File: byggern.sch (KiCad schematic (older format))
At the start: 41 parts, among them J1 Power_Rail, J2 JTAG LINK, J3 OLED_Connection, J4 CAN, J5 P1000 Header, J6 DB9_Female_MountingHoles, U1 Barrel_jack, U10 MAX233, U2 LM340SX, U3 ATmega162-16PU, U4 GAL16V8, U5 MCP2515, U6 SN74ALS573CN, U7 MCP2551, U8 IDT7164, U9 ADC0844, Y1 4.9MHz, Y2 16MHz

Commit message: Add footprints to components
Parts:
- D1: footprint (none) -> LED_SMD:LED_0805_2012Metric_Pad1.15x1.40mm_HandSolder
- J6: footprint (none) -> Connector_Dsub:DSUB-9_Female_Vertical_P2.77x2.84mm_MountingHoles
- U10: footprint (none) -> byggern:MAX233CPP
- U2: footprint (none) -> byggern:LM340SX
- U4: footprint (none) -> byggern:GAL16V8
- U5: footprint (none) -> byggern:MCP2515-EP
- U6: footprint (none) -> byggern:SN74ALS573CN
- U7: footprint (none) -> byggern:MCP2551-IP
- U8: footprint (none) -> byggern:CY7C185-20PC
- U9: footprint (none) -> byggern:ADC0844CCN
- Y1, Y2: footprint (none) -> Connector_PinHeader_2.54mm:PinHeader_1x02_P2.54mm_Vertical
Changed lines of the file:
@@
 F 0 "U2" H 1900 6975 50  0000 C CNN
 F 1 "LM340SX" H 1900 6884 50  0000 C CNN
-F 2 "" H 1800 6900 50  0001 C CNN
+F 2 "byggern:LM340SX" H 1800 6900 50  0001 C CNN
 F 3 "" H 1800 6900 50  0001 C CNN
 	1    1800 6900
@@
 F 0 "D1" V 2889 7132 50  0000 R CNN
 F 1 "PWR_LED" V 2798 7132 50  0000 R CNN
-F 2 "" H 2850 7250 50  0001 C CNN
+F 2 "LED_SMD:LED_0805_2012Metric_Pad1.15x1.40mm_HandSolder" H 2850 7250 50  0001 C CNN
 F 3 "~" H 2850 7250 50  0001 C CNN
 	1    2850 7250
@@
 F 0 "Y1" V 954 2381 50  0000 L CNN
 F 1 "4.9MHz" V 1045 2381 50  0000 L CNN
-F 2 "" H 1000 2250 50  0001 C CNN
+F 2 "Connector_PinHeader_2.54mm:PinHeader_1x02_P2.54mm_Vertical" H 1000 2250 50  0001 C CNN
 F 3 "~" H 1000 2250 50  0001 C CNN
 	1    1000 2250
@@
 F 0 "U10" H 10000 3450 50  0000 C CNN
 F 1 "MAX233" H 10100 3350 50  0000 C CNN
-F 2 "" H 9300 3450 50  0001 C CNN
+F 2 "byggern:MAX233CPP" H 9300 3450 50  0001 C CNN
 F 3 "" H 9300 3450 50  0001 C CNN
 	1    9550 3650
@@
 F 0 "J6" H 10700 6100 50  0000 L CNN
 F 1 "DB9_Female_MountingHoles" H 10700 6000 50  0000 L CNN
-F 2 "" H 11000 5400 50  0001 C CNN
+F 2 "Connector_Dsub:DSUB-9_Female_Vertical_P2.77x2.84mm_MountingHoles" H 11000 5400 50  0001 C CNN
 F 3 " ~" H 11000 5400 50  0001 C CNN
 	1    11000 5400
@@
 F 0 "U4" H 4450 4950 50  0000 C CNN
 F 1 "GAL16V8" H 4550 4850 50  0000 C CNN
-F 2 "" H 4350 4250 50  0001 C CNN
+F 2 "byggern:GAL16V8" H 4350 4250 50  0001 C CNN
 F 3 "" H 4350 4250 50  0001 C CNN
 	1    4350 4250
@@
 F 0 "U8" H 7050 2850 50  0000 L CNN
 F 1 "IDT7164" H 7050 2750 50  0000 L CNN
-F 2 "" H 6700 3150 50  0001 C CNN
+F 2 "byggern:CY7C185-20PC" H 6700 3150 50  0001 C CNN
 F 3 "" H 6700 3150 50  0001 C CNN
 	1    6700 2050
@@
 F 0 "U6" H 5700 1650 50  0000 C CNN
 F 1 "SN74ALS573CN" H 5900 1550 50  0000 C CNN
-F 2 "" H 5450 1450 50  0001 C CNN
+F 2 "byggern:SN74ALS573CN" H 5450 1450 50  0001 C CNN
 F 3 "" H 5450 1450 50  0001 C CNN
 	1    5450 1400
@@
 F 0 "U9" H 8750 1450 50  0000 C CNN
 F 1 "ADC0844" H 8850 1350 50  0000 C CNN
-F 2 "" H 8800 1350 50  0001 C CNN
+F 2 "byggern:ADC0844CCN" H 8800 1350 50  0001 C CNN
 F 3 "" H 8800 1350 50  0001 C CNN
 	1    8450 1350
@@
 F 0 "U5" H 4900 5650 50  0000 C CNN
 F 1 "MCP2515" H 5050 5550 50  0000 C CNN
-F 2 "" H 4700 5750 50  0001 C CNN
+F 2 "byggern:MCP2515-EP" H 4700 5750 50  0001 C CNN
 F 3 "" H 4700 5750 50  0001 C CNN
 	1    4700 5750
@@
 F 0 "Y2" V 3950 7250 50  0000 R CNN
 F 1 "16MHz" V 3850 7250 50  0000 R CNN
-F 2 "" H 3850 6900 50  0001 C CNN
+F 2 "Connector_PinHeader_2.54mm:PinHeader_1x02_P2.54mm_Vertical" H 3850 6900 50  0001 C CNN
 F 3 "~" H 3850 6900 50  0001 C CNN
 	1    3850 6900
@@
 F 0 "U7" H 6600 5150 50  0000 C CNN
 F 1 "MCP2551" H 6700 5050 50  0000 C CNN
-F 2 "" H 6350 5500 50  0001 C CNN
+F 2 "byggern:MCP2551-IP" H 6350 5500 50  0001 C CNN
 F 3 "" H 6350 5500 50  0001 C CNN
 	1    6350 5500

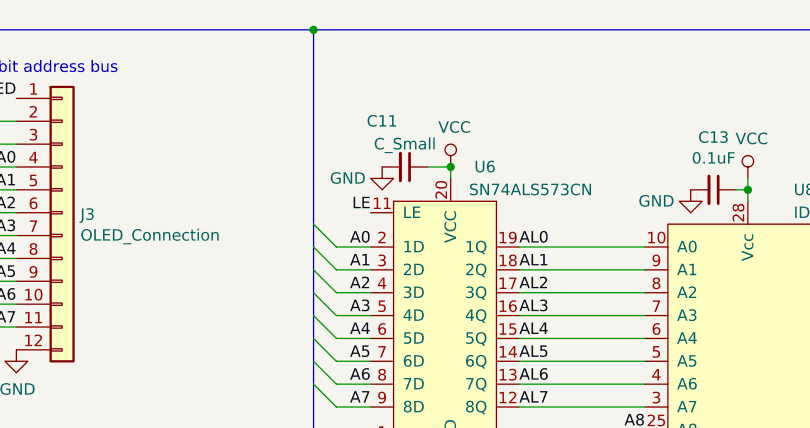
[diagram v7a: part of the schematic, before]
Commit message: Start routing PCB
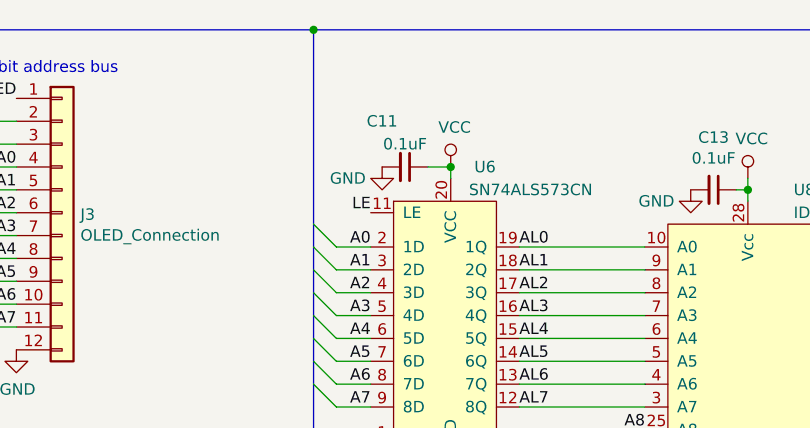
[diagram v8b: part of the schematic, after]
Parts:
- C11: value C_Small -> 0.1uF
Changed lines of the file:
@@
 P 5350 1150
 F 0 "C11" V 5150 1050 50  0000 C CNN
-F 1 "C_Small" V 5250 1150 50  0000 C CNN
+F 1 "0.1uF" V 5250 1150 50  0000 C CNN
 F 2 "Capacitor_SMD:C_0805_2012Metric_Pad1.15x1.40mm_HandSolder" H 5350 1150 50  0001 C CNN
 F 3 "~" H 5350 1150 50  0001 C CNN
